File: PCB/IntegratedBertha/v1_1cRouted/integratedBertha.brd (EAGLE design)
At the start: 108.1 x 84.6 mm, 100 parts, among them CON1 SPI, IC1 REG1117, IC2 AD8223, J7 22--02, Q1 BSP75, Q2 BSP75, Q4 BSP75, Q5 BSP75, Q6 BSP75, Q7 IRF3704S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

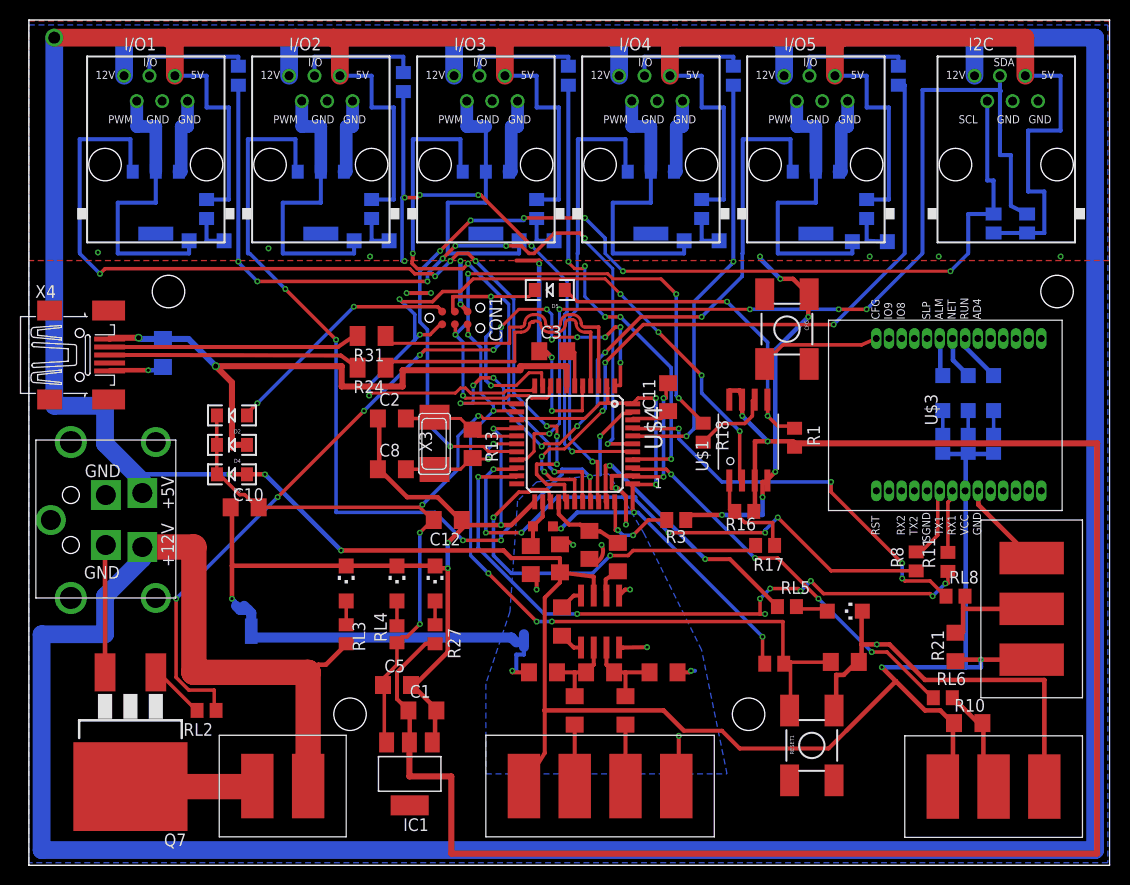
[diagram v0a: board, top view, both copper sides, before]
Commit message: corrected boards to fulfill design rules of the factory in Bogota (drill size and copper spacing. small changes in solardecathlon (SPI pins and design rules changed for zigbee header pads
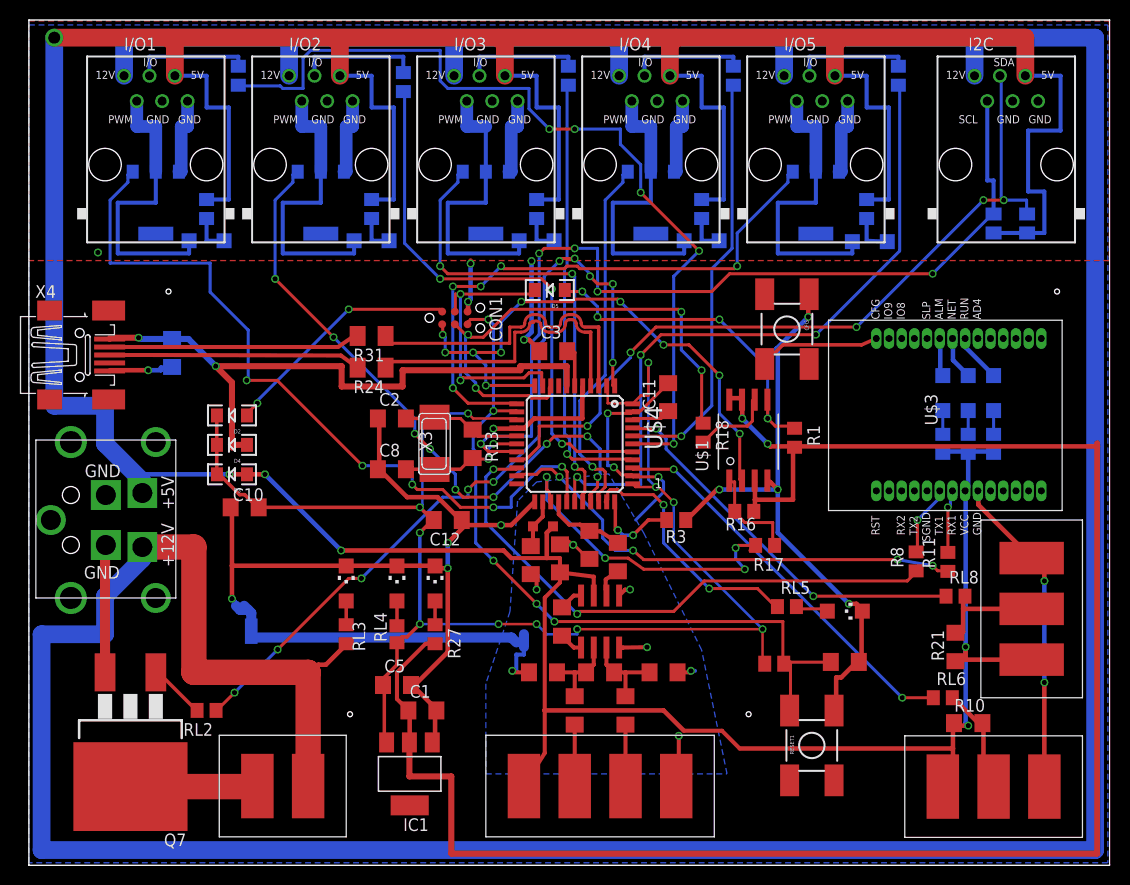
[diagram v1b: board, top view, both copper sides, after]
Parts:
- moved C7 0.91 mm to (14.3, 48.5)
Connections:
- net +5V: now also L1.2
- net +5V/1: no longer L1.2
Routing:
- net +5V/1: track 130.1 -> 155.9 mm, vias 9 -> 11
- net MISO: track 80.5 -> 57.8 mm, vias 7 -> 10
- net D10*: track 82.3 -> 63.9 mm, vias 5 -> 9
- net SDA: track 97.2 -> 78.8 mm
- net TX: track 66.1 -> 48.5 mm, vias 9 -> 4
- net D6*: track 94.6 -> 77.4 mm, vias 7 -> 5
- net D11*: track 71.7 -> 58.8 mm, vias 7 -> 5
- net GND: track 280.4 -> 268.1 mm, vias 26 -> 17
- net SCL: track 105.1 -> 93.1 mm, vias 7 -> 5
- net D5*: track 46.4 -> 36.9 mm
- net D9*: track 56.9 -> 47.7 mm
- net SCK: track 59.9 -> 51.2 mm, vias 5 -> 4
- net CS: track 39.8 -> 32.9 mm, vias 2 -> 4
- net A3: track 81.0 -> 87.9 mm, vias 8 -> 5
- net A2: track 61.2 -> 55.1 mm, vias 6 -> 3
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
